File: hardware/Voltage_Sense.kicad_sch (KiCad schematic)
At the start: 12 parts, among them U4 AMC1311QDWVRQ1, U5 AMC1311QDWVRQ1, U6 AMC1311QDWVRQ1

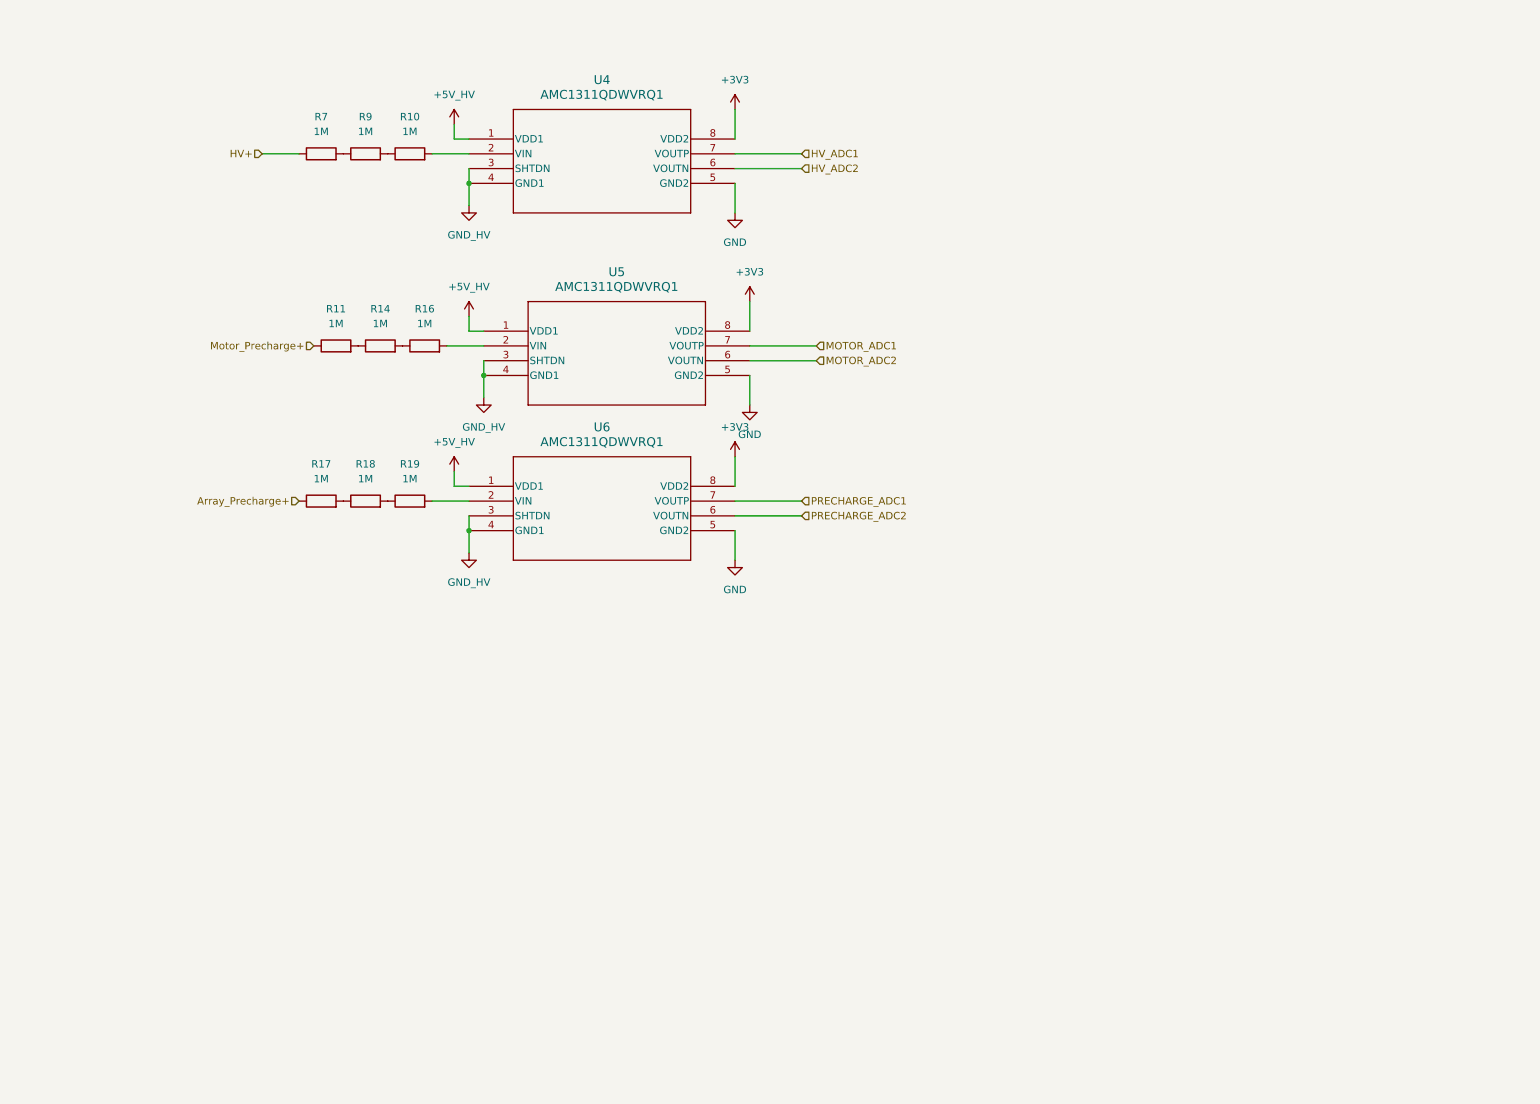
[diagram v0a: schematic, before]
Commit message: added designs for LZSR-80P and AMC class voltage sense
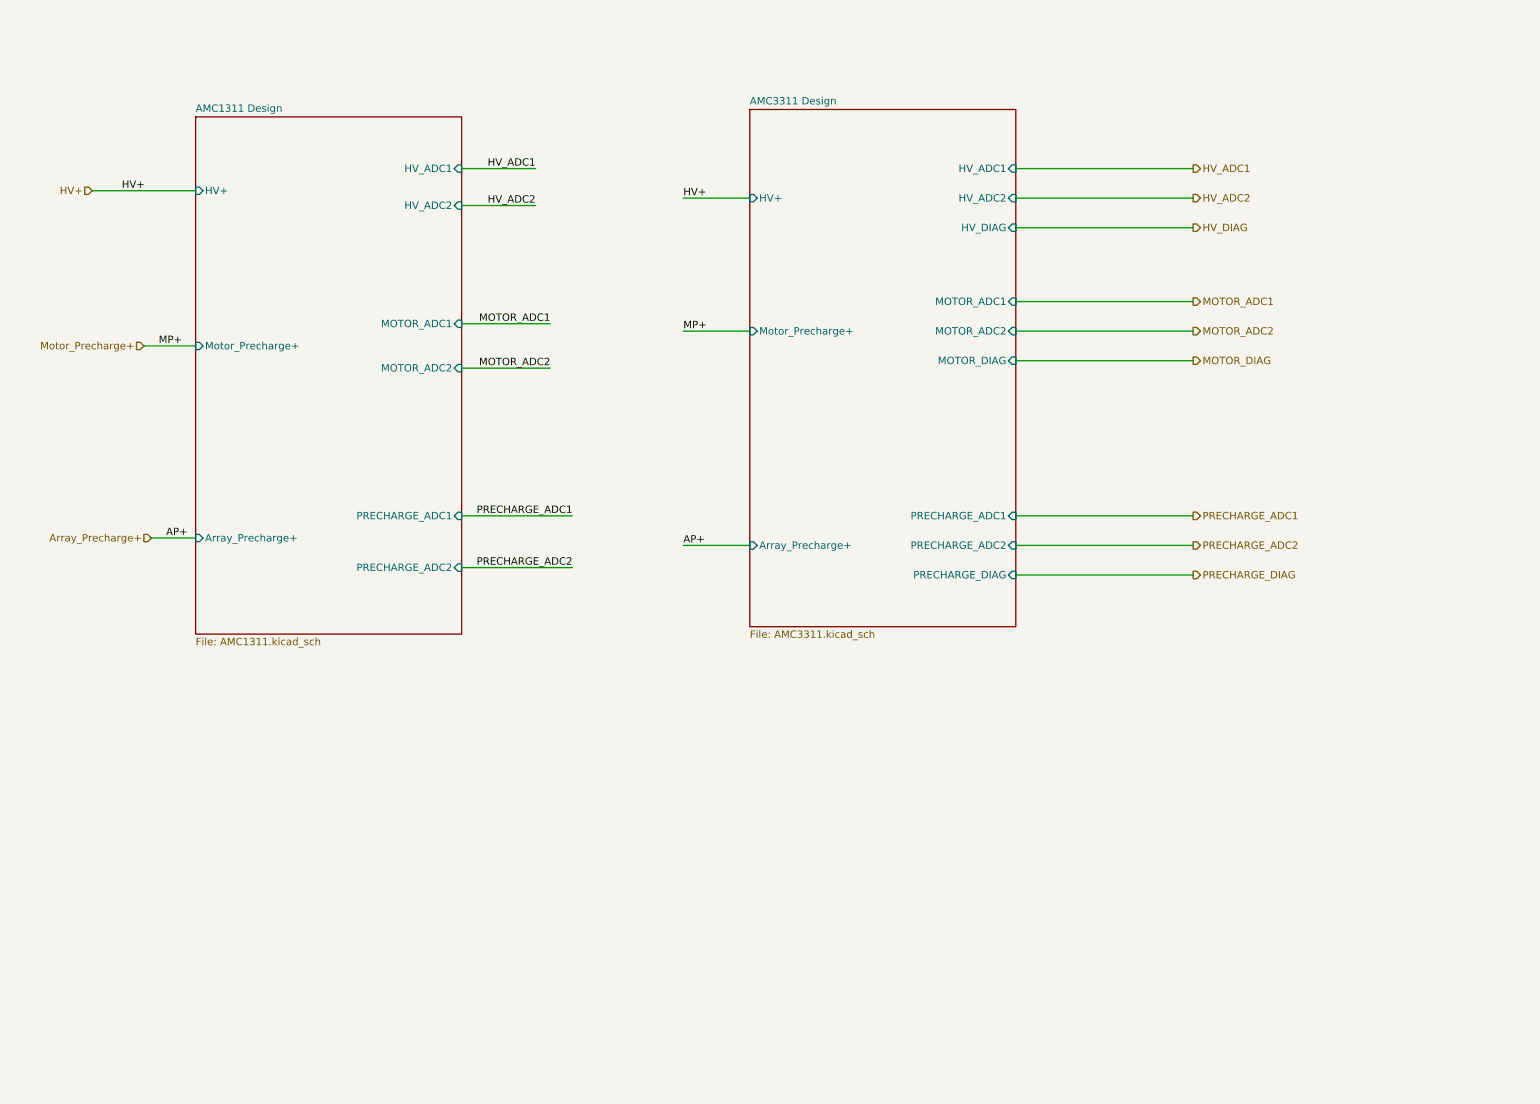
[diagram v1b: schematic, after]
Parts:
- removed R10, R11, R14, R16, R17, R18, R19, R7, R9: 1M, symbol Device:R
- removed U4, U5, U6: AMC1311QDWVRQ1, DWV8_TEX, symbol AMC1311QDWVRQ1:AMC1311QDWVRQ1
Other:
- added sheet AMC1311 Design (AMC1311.kicad_sch)
- added sheet AMC3311 Design (AMC3311.kicad_sch)

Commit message: labeled + stm32 cube layout
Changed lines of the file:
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@@
 	(wire
 		(pts
-			(xy 24.13 41.91) (xy 41.91 41.91)
+			(xy 31.75 41.91) (xy 41.91 41.91)
 		)
 		(stroke
@@
 	)
 	(label "HV+"
-		(at 29.21 41.91 0)
+		(at 35.56 41.91 0)
 		(effects
 			(font
@@
 	(hierarchical_label "HV+"
 		(shape input)
-		(at 24.13 41.91 180)
+		(at 31.75 41.91 180)
 		(effects
 			(font

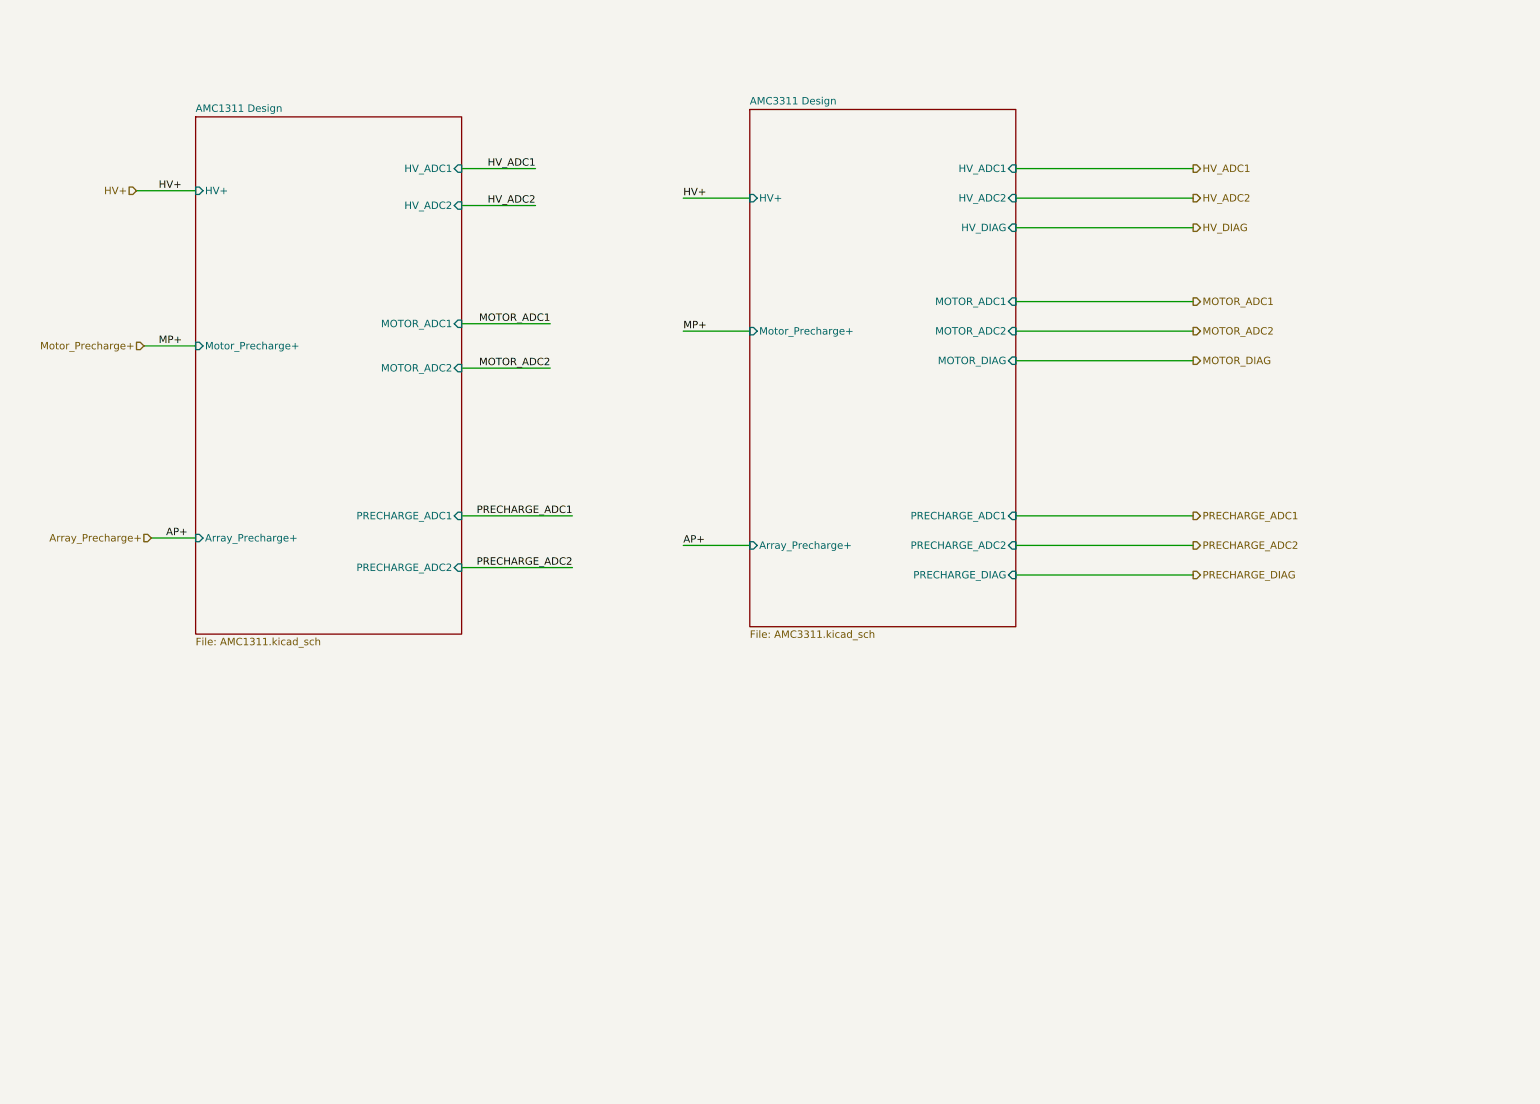
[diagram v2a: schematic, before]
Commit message: addressed 75% of review council 2, cleaned up ERC errors, embedded datasheet and PN
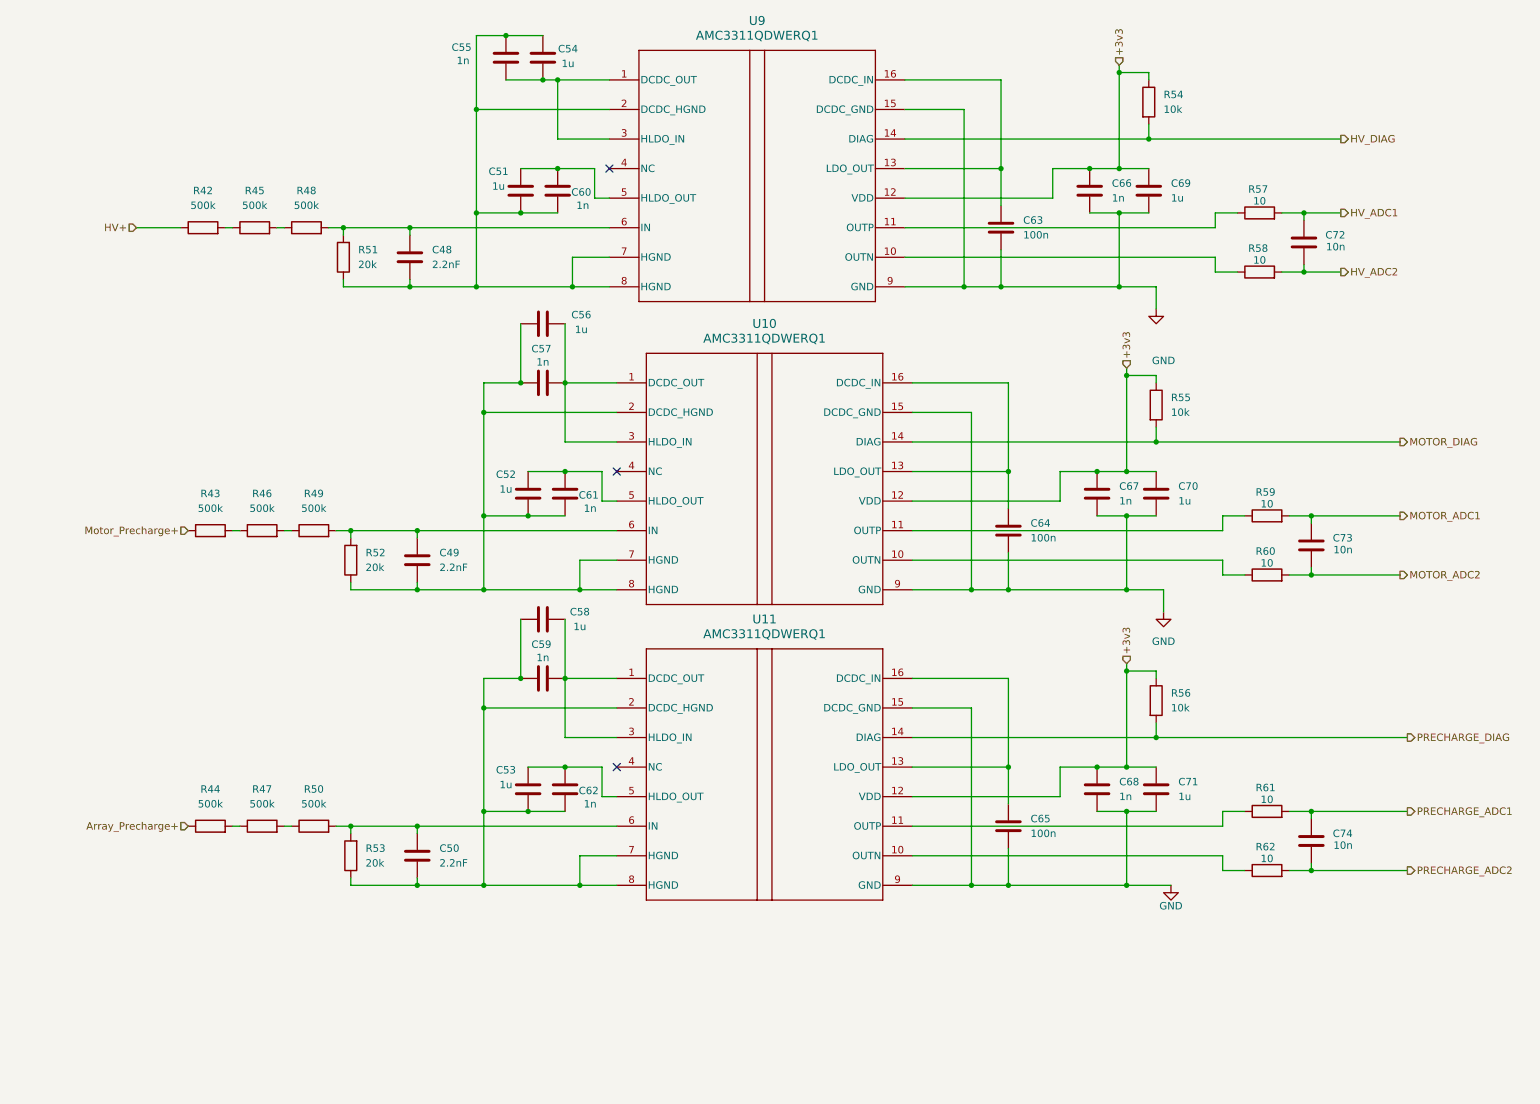
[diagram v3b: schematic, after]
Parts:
- added C48, C49, C50: 2.2nF, symbol Device:C
- added C51, C52, C53, C54, C56, C58, C69, C70, C71: 1u, symbol Device:C
- added C55, C57, C59, C60, C61, C62, C66, C67, C68: 1n, symbol Device:C
- added C63, C64, C65: 100n, symbol Device:C
- added C72, C73, C74: 10n, symbol Device:C
- added R42, R43, R44, R45, R46, R47, R48, R49, R50: 500k, symbol Device:R
- added R51, R52, R53: 20k, symbol Device:R
- added R54, R55, R56: 10k, symbol Device:R
- added R57, R58, R59, R60, R61, R62: 10, symbol Device:R
- added U10, U11, U9: AMC3311QDWERQ1, DWE0016A-IPC_A, symbol AMC3311QDWERQ1:AMC3311QDWERQ1
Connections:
- net Array_Precharge+: now also R44.1
- net HV+: now also R42.1
- net HV_ADC1: now also C72.2, R57.2
- net HV_ADC2: now also C72.1, R58.2
- net HV_DIAG: now also R54.2, U9.14 (DIAG)
- net MOTOR_ADC1: now also C73.2, R59.2
- net MOTOR_ADC2: now also C73.1, R60.2
- net MOTOR_DIAG: now also R55.2, U10.14 (DIAG)
- net Motor_Precharge+: now also R43.1
- net PRECHARGE_ADC1: now also C74.2, R61.2
- net PRECHARGE_ADC2: now also C74.1, R62.2
- net PRECHARGE_DIAG: now also R56.2, U11.14 (DIAG)
- new net: C48.2, C51.1, C54.1, C55.2, C60.1, R51.1, U9.2 (DCDC_HGND), U9.7 (HGND), U9.8 (HGND)
- new net: C51.2, C60.2, U9.5 (HLDO_OUT)
- new net: C49.2, C52.1, C56.1, C57.1, C61.1, R52.1, U10.2 (DCDC_HGND), U10.7 (HGND), U10.8 (HGND)
- new net: C56.2, C57.2, U10.1 (DCDC_OUT), U10.3 (HLDO_IN)
- new net: C50.2, C53.1, C58.1, C59.1, C62.1, R53.1, U11.2 (DCDC_HGND), U11.7 (HGND), U11.8 (HGND)
- new net: C53.2, C62.2, U11.5 (HLDO_OUT)
- new net: C64.1, U10.13 (LDO_OUT), U10.16 (DCDC_IN)
- new net: R60.1, U10.10 (OUTN)
- new net: R59.1, U10.11 (OUTP)
- new net: C52.2, C61.2, U10.5 (HLDO_OUT)
- new net: C49.1, R49.2, R52.2, U10.6 (IN)
- new net: R47.2, R50.1
- new net: C50.1, R50.2, R53.2, U11.6 (IN)
- new net: C58.2, C59.2, U11.1 (DCDC_OUT), U11.3 (HLDO_IN)
- new net: R46.2, R49.1
- new net: R42.2, R45.1
- new net: R45.2, R48.1
- new net: R58.1, U9.10 (OUTN)
- new net: C48.1, R48.2, R51.2, U9.6 (IN)
- new net: R61.1, U11.11 (OUTP)
- new net: C63.1, U9.13 (LDO_OUT), U9.16 (DCDC_IN)
- new net: R44.2, R47.1
- new net: R62.1, U11.10 (OUTN)
- new net: C65.1, U11.13 (LDO_OUT), U11.16 (DCDC_IN)
- new net: R43.2, R46.1
- new net: C54.2, C55.1, U9.1 (DCDC_OUT), U9.3 (HLDO_IN)
- new net: R57.1, U9.11 (OUTP)
- new net +3v3: C66.1, C67.1, C68.1, C69.1, C70.1, C71.1, R54.1, R55.1, R56.1, U10.12 (VDD), U11.12 (VDD), U9.12 (VDD)
- new net GND: C63.2, C64.2, C65.2, C66.2, C67.2, C68.2, C69.2, C70.2, C71.2, U10.15 (DCDC_GND), U10.9 (GND), U11.15 (DCDC_GND), U11.9 (GND), U9.15 (DCDC_GND), U9.9 (GND)
- no-connect marks 0 -> 3
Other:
- removed sheet AMC1311 Design
- removed sheet AMC3311 Design

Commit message: added calcs, cleaned up, addressed comments
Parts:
- removed C50: 2.2nF, symbol Device:C
- removed C58, C71: 1u, symbol Device:C
- removed C59, C62, C68: 1n, symbol Device:C
- removed C65: 100n, symbol Device:C
- removed C74: 10n, symbol Device:C
- removed R44, R47, R50: 500k, symbol Device:R
- removed R56: 10k, symbol Device:R
- removed R61, R62: 10, symbol Device:R
- removed U11: AMC3311QDWERQ1, DWE0016A-IPC_A, symbol AMC3311QDWERQ1:AMC3311QDWERQ1
- added C42: 1n, symbol Device:C
- added C60: 0.1u, symbol Device:C
- added D19, D20, D21, D22: TVS, Diode_SMD:D_SOD-123F, symbol Device:D_Zener
- added R42, R43, R48, R54: 10k, symbol Device:R
- added R55: 20k, symbol Device:R
- added TP17: MOTOR_ADC, symbol Connector:TestPoint
- added TP18: HV_ADC, symbol Connector:TestPoint
- added TP19: HV_DIAG, symbol Connector:TestPoint
- added TP20: HV_OUTP, symbol Connector:TestPoint
- added TP21: HV_OUTN, symbol Connector:TestPoint
- added TP22: Motor_DIAG, symbol Connector:TestPoint
- added TP23: Motor_OUTP, symbol Connector:TestPoint
- added TP24: Motor_OUTN, symbol Connector:TestPoint
- added U6: TLV9002QDRQ1, Package_SO:SOIC-8_3.9x4.9mm_P1.27mm, symbol lhrs_misc:TLV9002QDRQ1
- C53: value 1u -> 1n
- R53: value 20k -> 10k
- renumbered C48 to C43, C49 to C44, C55 to C45, C51 to C46, C52 to C47, C54 to C48, C56 to C49, C57 to C50, C60 to C51, C61 to C52, C63 to C54, C64 to C55, C66 to C56, C67 to C57, C69 to C58, C70 to C59, C72 to C61, C73 to C62, R42 to R44, R43 to R45, R45 to R46, R46 to R47, R48 to R49, R49 to R50, R54 to R56, R55 to R57, R57 to R58, R58 to R59, R59 to R60, R60 to R61, U9 to U7, U10 to U8
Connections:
- net +3v3: now also C60.1, D19.1 (K), D21.1 (K), U6.8 (V+)
- net GND: now also C60.2, D20.2 (A), D22.2 (A), U6.4 (V-)
- net HV_DIAG: now also TP19.1
- net MOTOR_DIAG: now also TP22.1
- net HV_ADC: now reaches C53.1
- net HV_ADC: now also D21.2 (A), D22.1 (K), R55.2, TP18.1, U6.7; no longer R53.1
- net at C53.2: now also R53.2, R55.1, U6.6 (-)
- net HV_ADC1 renamed HV_OUTP
- net HV_OUTP: now also R54.1, TP20.1
- net HV_ADC2 renamed HV_OUTN
- net HV_OUTN: now also R53.1, TP21.1
- net MOTOR_ADC1 renamed MOTOR_OUTP
- net MOTOR_OUTP: now also R43.1, TP23.1
- net MOTOR_ADC2 renamed MOTOR_OUTN
- net MOTOR_OUTN: now also R42.1, TP24.1
- new net: C42.2, R42.2, R48.1, U6.2 (-)
- new net: R43.2, U6.3 (+)
- new net: R54.2, U6.5 (+)
- new net MOTOR_ADC: C42.1, D19.2 (A), D20.1 (K), R48.2, TP17.1, U6.1
- no-connect marks 3 -> 2
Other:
- note added: "AMC3311 ADC Output Calc"
- note added: "Ratio = V_AMC3311_MAX / V_HV_MAX = 2.0V/140V = 0.014286V/V Op_amp_gain = 1.0 V_Out_Diff = = Vin_HV * Ratio * Op_amp_gain = Vin_HV * 0.014286 * 1 V_ADC = V_Out_Diff * Op_amp_gain"
- note added: "Vin_HV = Motor_ADC = Precharge_ADC 0V = 0V 35V = 0.5V 70V = 1V 105V = 1.5V 140V = 2.0V"
